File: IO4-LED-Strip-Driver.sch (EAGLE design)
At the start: 21 parts, among them Q1 DMN4468, Q2 DMN4468, Q3 DMN4468, Q7 DMN4468

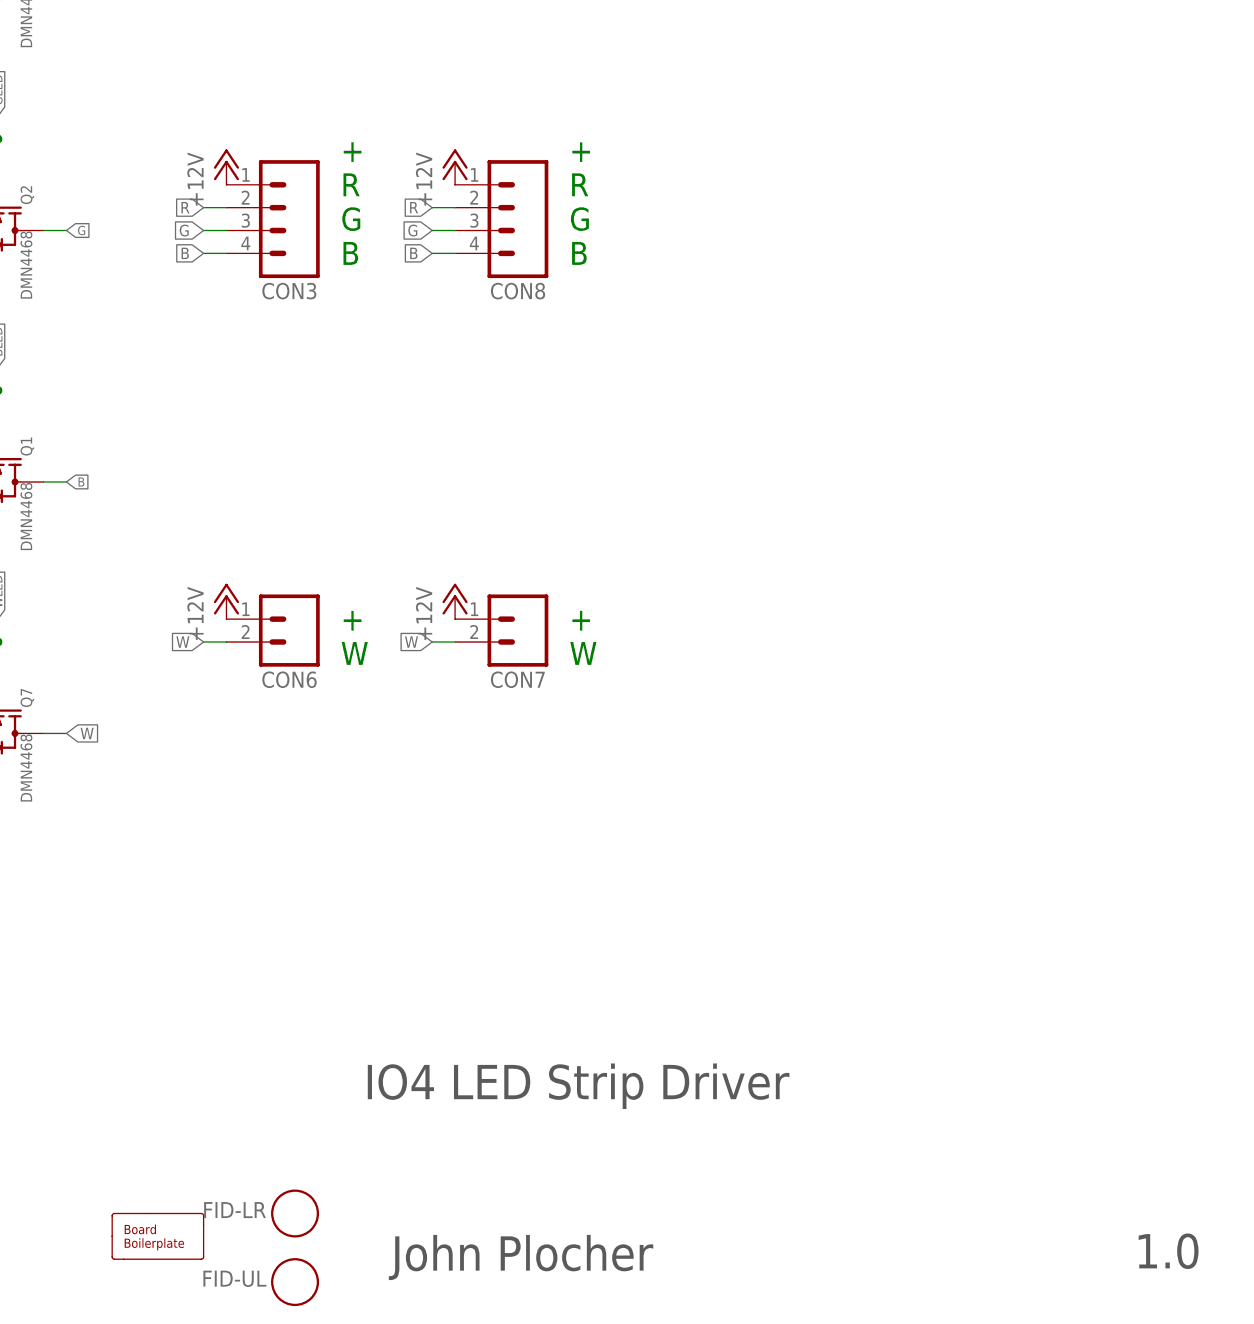
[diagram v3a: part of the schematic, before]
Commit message: Swapped R and G connector locations to match LED string wiring
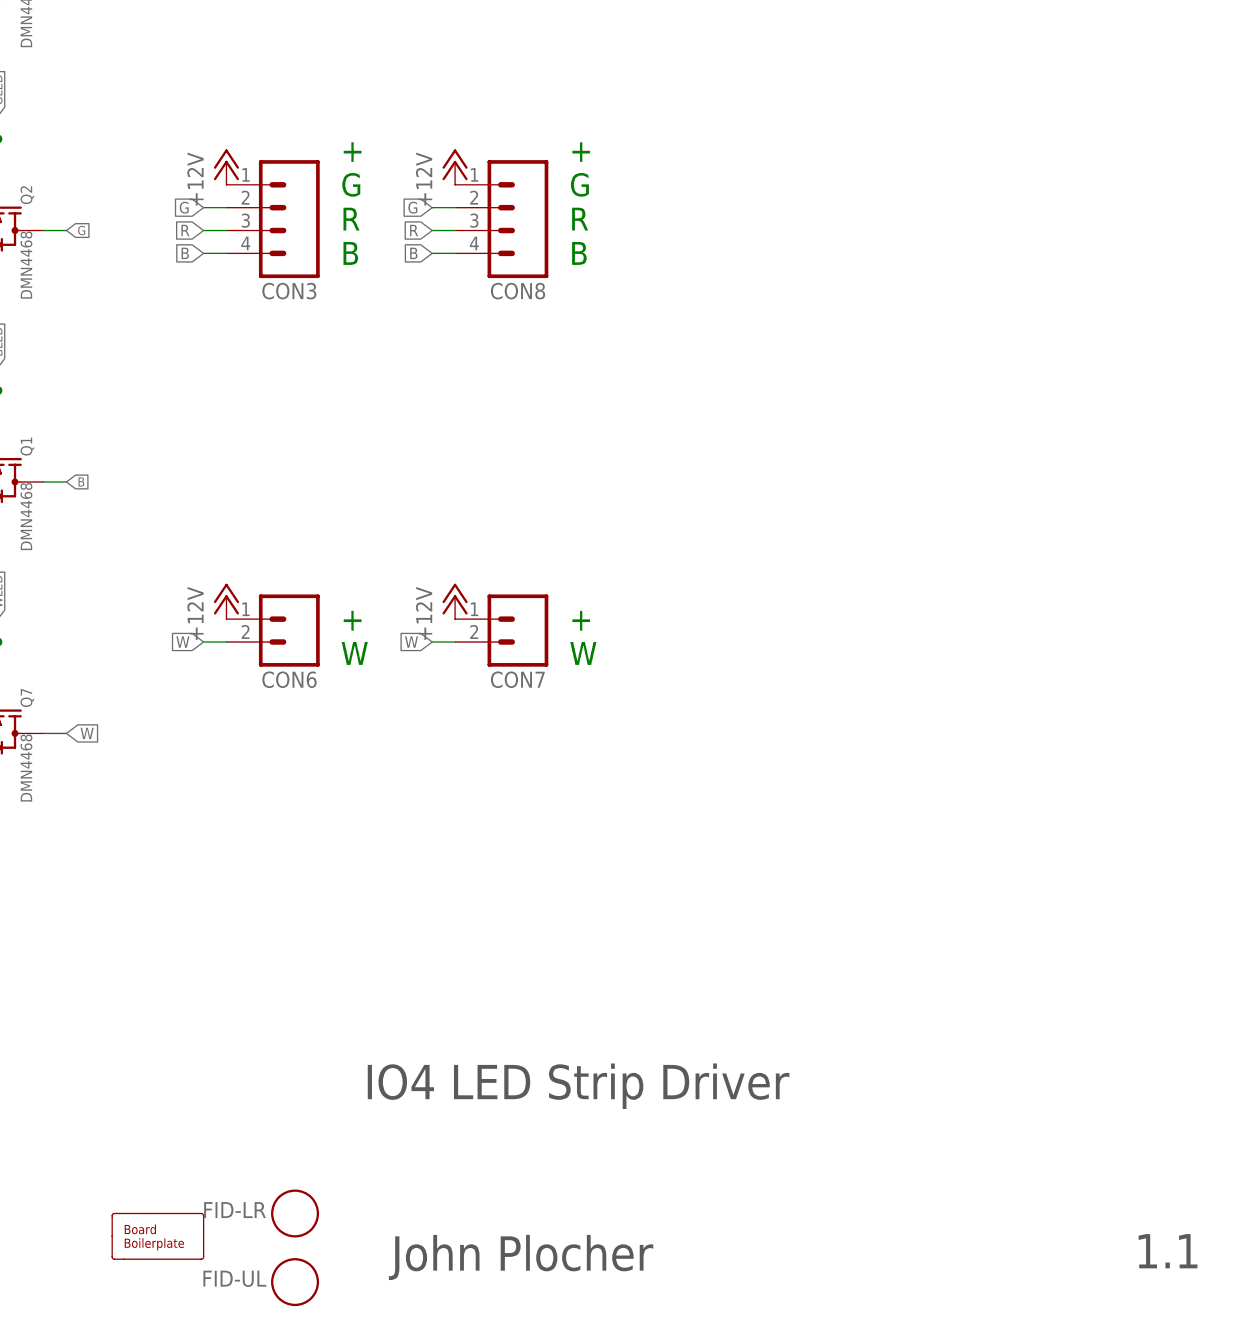
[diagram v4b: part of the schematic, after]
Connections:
- net G: now also CON3.2, CON8.2; no longer CON3.3, CON8.3
- net R: now also CON3.3, CON8.3; no longer CON3.2, CON8.2
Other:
- note added: "+ G R B"
- note added: "1.1"
- note added: "Drives 2x RGB strips and 2x White strips with a 12v/15A power supply (For backdrop and valence controlled lighting) V1.1 - LED Strips are GRB, not RGB - changed connector mapping to match"
- note removed: "+ R G B"
- note removed: "1.0"
- note removed: "Drives 2x RGB strips and 2x White strips with a 12v/15A power supply (For backdrop and valence controlled lighting)"
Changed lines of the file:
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@@
 <text x="149.86" y="25.4" size="3.81" layer="97">IO4 LED Strip Driver</text>
 <text x="152.908" y="6.35" size="3.81" layer="97">John Plocher</text>
-<text x="235.458" y="6.604" size="3.81" layer="97">1.0</text>
-<text x="147.32" y="38.1" size="1.6764" layer="102">Drives 2x RGB strips and 2x White strips with a 12v/15A power supply
-(For backdrop and valence controlled lighting)</text>
+<text x="235.458" y="6.604" size="3.81" layer="97">1.1</text>
+<text x="139.7" y="38.1" size="1.6764" layer="102">Drives 2x RGB strips and 2x White strips with a 12v/15A power supply
+(For backdrop and valence controlled lighting)
+V1.1 - LED Strips are GRB, not RGB - changed connector mapping to match</text>
 <text x="147.32" y="118.11" size="2.54" layer="91">+
+G
 R
-G
 B</text>
 <text x="147.32" y="73.66" size="2.54" layer="91">+
@@
 W</text>
 <text x="172.72" y="118.11" size="2.54" layer="91">+
+G
 R
-G
 B</text>
 </plain>
@@
 <net name="R" class="0">
 <segment>
+<pinref part="Q3" gate="Q" pin="D"/>
+<wire x1="114.3" y1="149.86" x2="116.84" y2="149.86" width="0.1524" layer="91"/>
+<label x="116.84" y="149.86" size="1.016" layer="95" xref="yes"/>
+</segment>
+<segment>
+<pinref part="CON3" gate="J" pin="3"/>
+<wire x1="134.62" y1="121.92" x2="132.08" y2="121.92" width="0.1524" layer="91"/>
+<label x="132.08" y="121.92" size="1.27" layer="95" rot="R180" xref="yes"/>
+</segment>
+<segment>
+<pinref part="CON8" gate="J" pin="3"/>
+<wire x1="160.02" y1="121.92" x2="157.48" y2="121.92" width="0.1524" layer="91"/>
+<label x="157.48" y="121.92" size="1.27" layer="95" rot="R180" xref="yes"/>
+</segment>
+</net>
+<net name="G" class="0">
+<segment>
+<pinref part="Q2" gate="Q" pin="D"/>
+<wire x1="114.3" y1="121.92" x2="116.84" y2="121.92" width="0.1524" layer="91"/>
+<label x="116.84" y="121.92" size="1.016" layer="95" xref="yes"/>
+</segment>
+<segment>
 <pinref part="CON3" gate="J" pin="2"/>
 <wire x1="134.62" y1="124.46" x2="132.08" y2="124.46" width="0.1524" layer="91"/>
@@
 </segment>
 <segment>
-<pinref part="Q3" gate="Q" pin="D"/>
-<wire x1="114.3" y1="149.86" x2="116.84" y2="149.86" width="0.1524" layer="91"/>
-<label x="116.84" y="149.86" size="1.016" layer="95" xref="yes"/>
-</segment>
-<segment>
 <pinref part="CON8" gate="J" pin="2"/>
 <wire x1="160.02" y1="124.46" x2="157.48" y2="124.46" width="0.1524" layer="91"/>
@@
 </segment>
 </net>
-<net name="G" class="0">
-<segment>
-<pinref part="CON3" gate="J" pin="3"/>
-<wire x1="134.62" y1="121.92" x2="132.08" y2="121.92" width="0.1524" layer="91"/>
-<label x="132.08" y="121.92" size="1.27" layer="95" rot="R180" xref="yes"/>
-</segment>
-<segment>
-<pinref part="Q2" gate="Q" pin="D"/>
-<wire x1="114.3" y1="121.92" x2="116.84" y2="121.92" width="0.1524" layer="91"/>
-<label x="116.84" y="121.92" size="1.016" layer="95" xref="yes"/>
-</segment>
-<segment>
-<pinref part="CON8" gate="J" pin="3"/>
-<wire x1="160.02" y1="121.92" x2="157.48" y2="121.92" width="0.1524" layer="91"/>
-<label x="157.48" y="121.92" size="1.27" layer="95" rot="R180" xref="yes"/>
-</segment>
-</net>

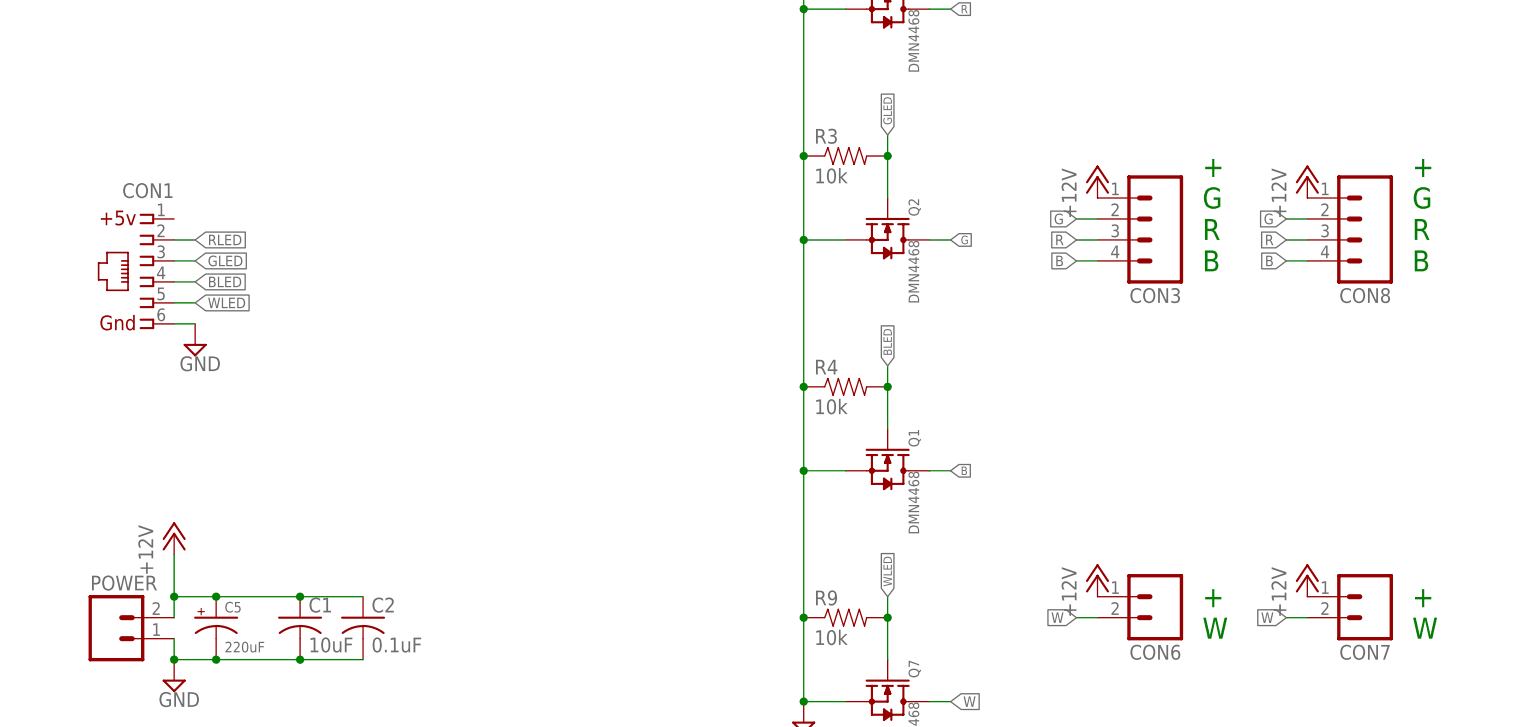
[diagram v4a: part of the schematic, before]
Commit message: added values for connectors
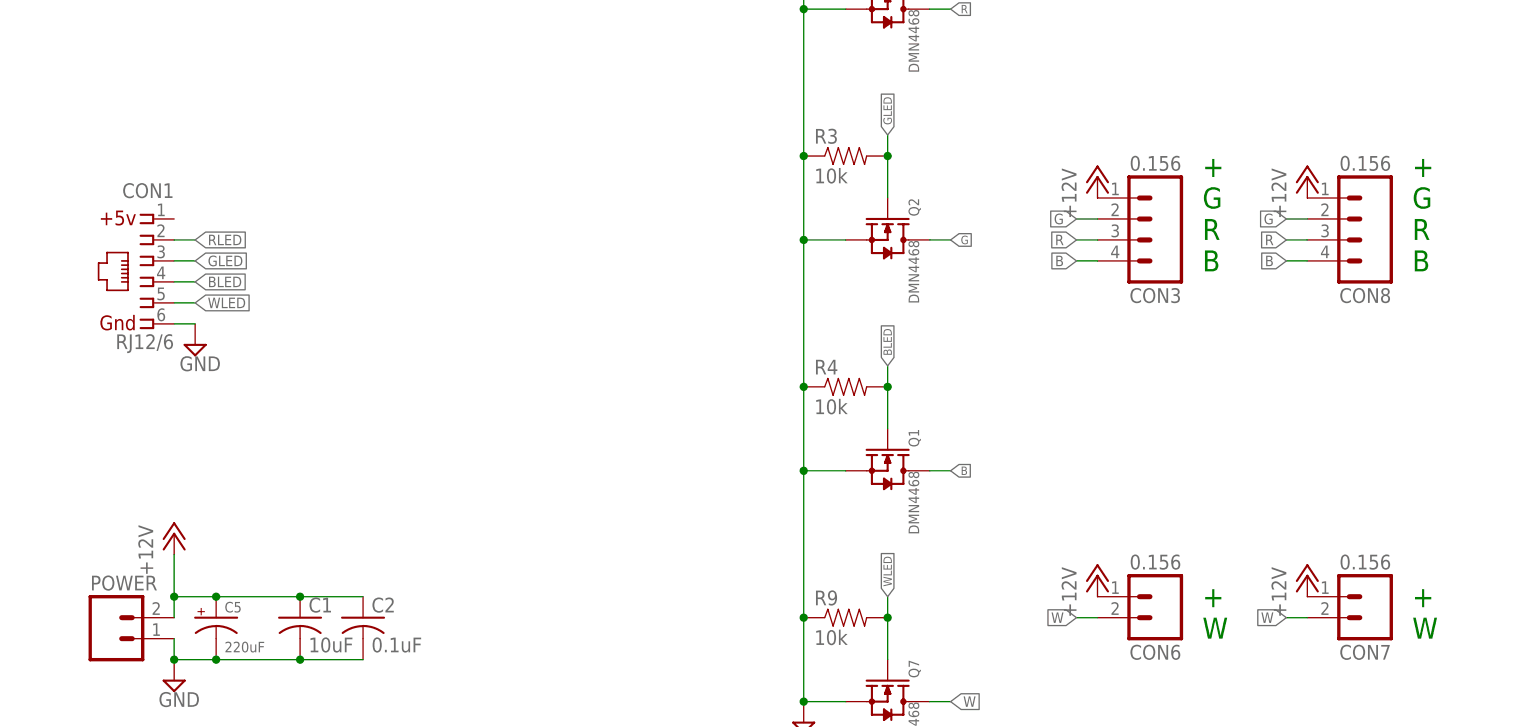
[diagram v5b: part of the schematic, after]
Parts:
- CON1: value (none) -> RJ12/6
- CON3, CON6, CON7, CON8: value (none) -> 0.156
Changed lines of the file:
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@@
 <part name="Q7" library="SPCoast" deviceset="MOSFET-N-*-?" device="SO8" value="DMN4468"/>
 <part name="V29" library="supply2" deviceset="GND" device=""/>
-<part name="CON3" library="SPCoast" deviceset="CONNECTOR-M04" device="5.08"/>
+<part name="CON3" library="SPCoast" deviceset="CONNECTOR-M04" device="5.08" value="0.156"/>
 <part name="POWER" library="SPCoast" deviceset="CONNECTOR-M02" device="MSTBA2"/>
 <part name="R5" library="SPCoast" deviceset="R*" device="0603-RES" value="10k"/>
@@
 <part name="R4" library="SPCoast" deviceset="R*" device="0603-RES" value="10k"/>
 <part name="R9" library="SPCoast" deviceset="R*" device="0603-RES" value="10k"/>
-<part name="CON1" library="SPCoast" deviceset="CONNECTOR-IO4" device="INV"/>
+<part name="CON1" library="SPCoast" deviceset="CONNECTOR-IO4" device="INV" value="RJ12/6"/>
 <part name="V1" library="supply2" deviceset="GND" device=""/>
 <part name="V2" library="supply2" deviceset="GND" device=""/>
-<part name="CON6" library="SPCoast" deviceset="CONNECTOR-M02" device="MSTBA2"/>
+<part name="CON6" library="SPCoast" deviceset="CONNECTOR-M02" device="MSTBA2" value="0.156"/>
 <part name="P+5" library="SPCoast" deviceset="+12V" device=""/>
-<part name="CON7" library="SPCoast" deviceset="CONNECTOR-M02" device="MSTBA2"/>
+<part name="CON7" library="SPCoast" deviceset="CONNECTOR-M02" device="MSTBA2" value="0.156"/>
 <part name="P+6" library="SPCoast" deviceset="+12V" device=""/>
 <part name="P+8" library="SPCoast" deviceset="+12V" device=""/>
-<part name="CON8" library="SPCoast" deviceset="CONNECTOR-M04" device="5.08"/>
+<part name="CON8" library="SPCoast" deviceset="CONNECTOR-M04" device="5.08" value="0.156"/>
 <part name="FID-UL" library="SPCoast" deviceset="FIDUCIAL" device=""/>
 <part name="FID-LR" library="SPCoast" deviceset="FIDUCIAL" device=""/>

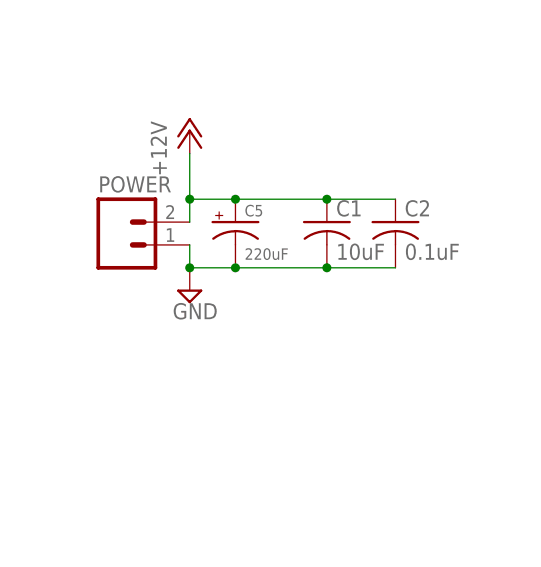
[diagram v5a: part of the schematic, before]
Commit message: added values for connectors
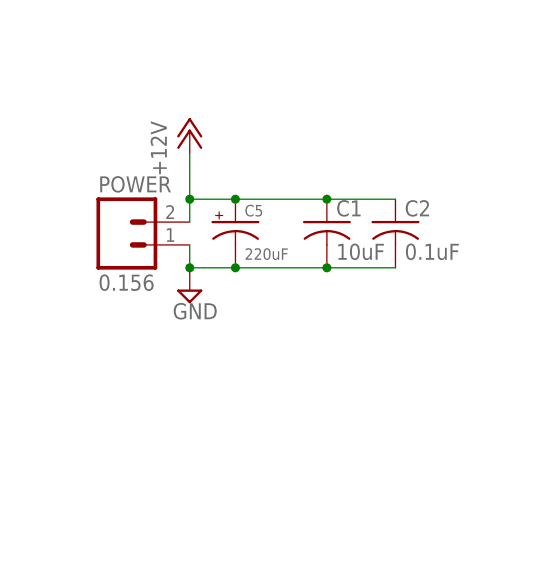
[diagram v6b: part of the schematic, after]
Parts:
- POWER: value (none) -> 0.156
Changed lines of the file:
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@@
 <part name="V29" library="supply2" deviceset="GND" device=""/>
 <part name="CON3" library="SPCoast" deviceset="CONNECTOR-M04" device="5.08" value="0.156"/>
-<part name="POWER" library="SPCoast" deviceset="CONNECTOR-M02" device="MSTBA2"/>
+<part name="POWER" library="SPCoast" deviceset="CONNECTOR-M02" device="MSTBA2" value="0.156"/>
 <part name="R5" library="SPCoast" deviceset="R*" device="0603-RES" value="10k"/>
 <part name="R3" library="SPCoast" deviceset="R*" device="0603-RES" value="10k"/>

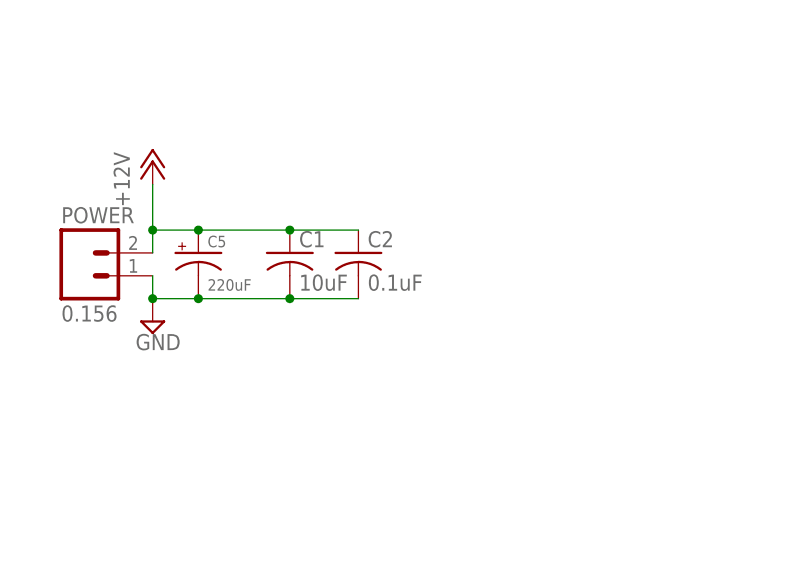
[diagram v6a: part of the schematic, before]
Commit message: normalized values
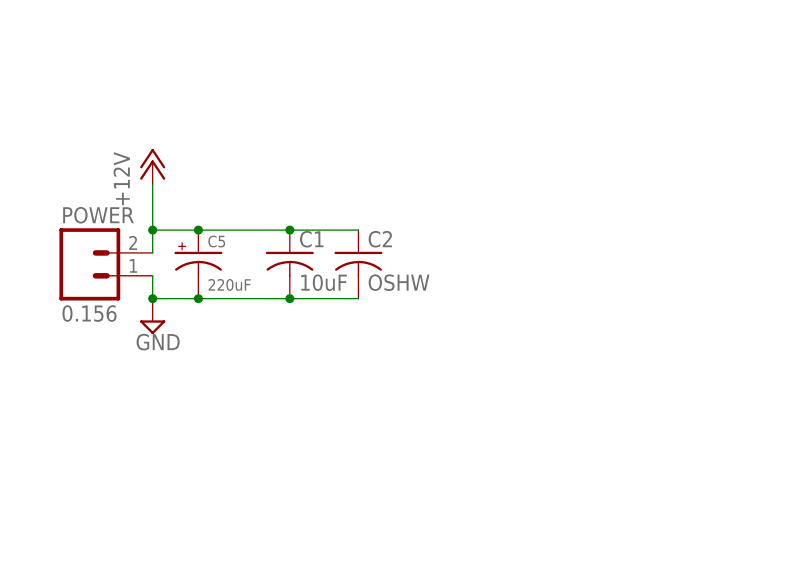
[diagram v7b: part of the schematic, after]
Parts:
- BOARD1: value BOARD80X100 -> BOARD
- C2: value 0.1uF -> OSHW
- OSHW1: value OSHW-LOGOL -> OSHW
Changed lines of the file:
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@@
 </classes>
 <parts>
-<part name="BOARD1" library="SPCoast" deviceset="BOARD" device="80X100" value="BOARD80X100"/>
+<part name="BOARD1" library="SPCoast" deviceset="BOARD" device="80X100" value="BOARD"/>
 <part name="FRAME2" library="MCP" deviceset="FRAME-LETTER" device=""/>
-<part name="OSHW1" library="SparkFun" deviceset="OSHW-LOGO" device="L" value="OSHW-LOGOL"/>
+<part name="OSHW1" library="SparkFun" deviceset="OSHW-LOGO" device="L" value="OSHW"/>
 <part name="C5" library="SPCoast" deviceset="CAP-POL*" device="0810" value="220uF"/>
 <part name="P+2" library="SPCoast" deviceset="+12V" device=""/>
@@
 <part name="FID-LR" library="SPCoast" deviceset="FIDUCIAL" device=""/>
 <part name="C1" library="SPCoast" deviceset="CAP*" device="0603" value="10uF"/>
-<part name="C2" library="SPCoast" deviceset="CAP*" device="0603" value="0.1uF"/>
+<part name="C2" library="SPCoast" deviceset="CAP*" device="0603" value="OSHW"/>
 </parts>
 <sheets>
